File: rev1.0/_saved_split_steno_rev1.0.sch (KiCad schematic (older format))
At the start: 45 parts, among them J0 Audio-Jack-4, K0 KEYSW, K1 KEYSW, K10 KEYSW, K11 KEYSW, K12 KEYSW, K13 KEYSW, K14 KEYSW, K15 KEYSW, K16 KEYSW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

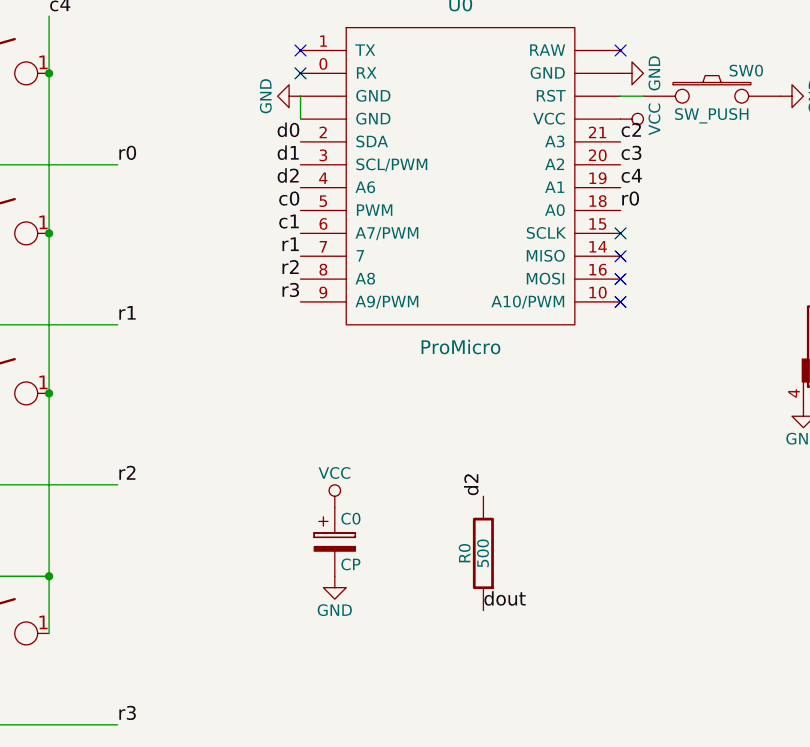
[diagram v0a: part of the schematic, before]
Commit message: reorganized schematic library and pro micro footprint
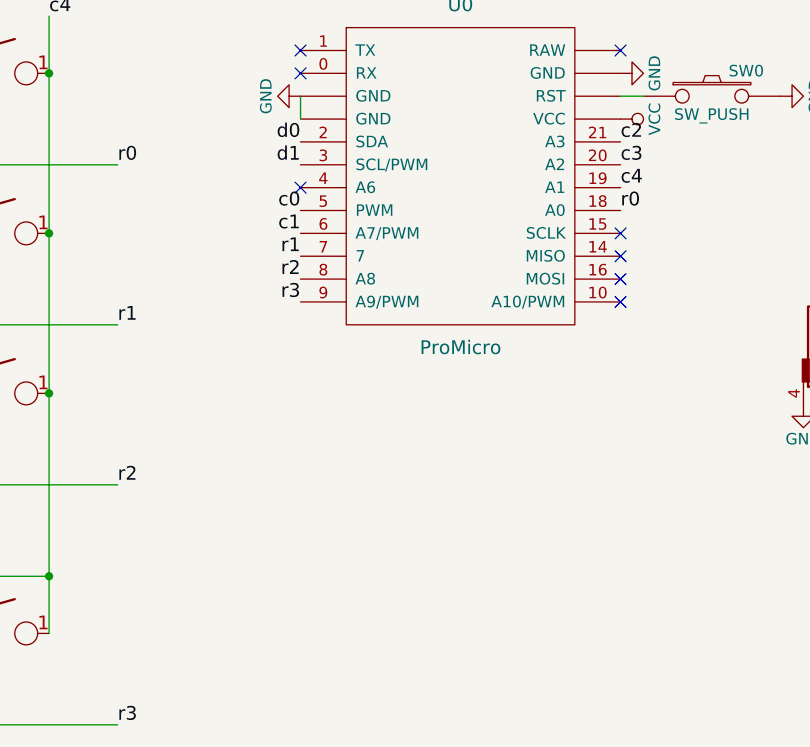
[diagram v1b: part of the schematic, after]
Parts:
- removed C0: CP, Capacitors_THT:CP_Radial_D4.0mm_P2.00mm, symbol CP
- removed R0: 500, Keebio-Parts:Resistor-Hybrid, symbol R
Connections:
- net d2: no longer names the net of U0.4 (A6)
- no-connect marks 7 -> 8
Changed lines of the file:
@@
 EESchema Schematic File Version 2
 LIBS:split_steno_rev1.0
-LIBS:keyboard_parts
-LIBS:ws2812b
-LIBS:promicro
 LIBS:power
 LIBS:device
@@
 Text Label 7050 1550 2    60   ~ 0
 d1
-Text Label 7850 3000 1    60   ~ 0
-d2
-$Comp
-L R R0
-U 1 1 5A98D003
-P 7850 3250
-F 0 "R0" V 7930 3250 50  0000 C CNN
-F 1 "500" V 7850 3250 50  0000 C CNN
-F 2 "Keebio-Parts:Resistor-Hybrid" H 7850 3250 60  0001 C CNN
-F 3 "" H 7850 3250 60  0000 C CNN
-	1    7850 3250
-	-1   0    0    1
-$EndComp
-Text Label 7050 1650 2    60   ~ 0
-d2
 Wire Wire Line
 	3250 1950 3250 1850
@@
 Connection ~ 5250 2950
 Connection ~ 5250 4000
-$Comp
-L CP C0
-U 1 1 5AA06AA7
-P 7200 3200
-F 0 "C0" H 7225 3300 50  0000 L CNN
-F 1 "CP" H 7225 3100 50  0000 L CNN
-F 2 "Capacitors_THT:CP_Radial_D4.0mm_P2.00mm" H 7238 3050 50  0001 C CNN
-F 3 "" H 7200 3200 50  0001 C CNN
-	1    7200 3200
-	1    0    0    -1
-$EndComp
-$Comp
-L VCC #PWR07
-U 1 1 5AA06BB0
-P 7200 3050
-F 0 "#PWR07" H 7200 2900 50  0001 C CNN
-F 1 "VCC" H 7200 3200 50  0000 C CNN
-F 2 "" H 7200 3050 50  0001 C CNN
-F 3 "" H 7200 3050 50  0001 C CNN
-	1    7200 3050
-	1    0    0    -1
-$EndComp
-$Comp
-L GND #PWR08
-U 1 1 5AA06C4D
-P 7200 3350
-F 0 "#PWR08" H 7200 3100 50  0001 C CNN
-F 1 "GND" H 7200 3200 50  0000 C CNN
-F 2 "" H 7200 3350 50  0001 C CNN
-F 3 "" H 7200 3350 50  0001 C CNN
-	1    7200 3350
-	1    0    0    -1
-$EndComp
-Text Label 7850 3500 0    60   ~ 0
-dout
 Wire Wire Line
 	7050 1350 7050 1250
@@
 	1    0    0    -1
 $EndComp
-NoConn ~ 8450 1850
 NoConn ~ 8450 1950
 NoConn ~ 8450 2050
@@
 NoConn ~ 7050 1050
 NoConn ~ 7050 1150
+NoConn ~ 7050 1650
+NoConn ~ 8450 1850
 $EndSCHEMATC
